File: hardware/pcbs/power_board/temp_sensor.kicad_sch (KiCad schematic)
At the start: 2 parts, among them U14 TMP1075D

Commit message: power_board: final version
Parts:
- C39: LCSC (none) -> C49678
- U14: LCSC (none) -> C2878381
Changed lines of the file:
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@@
+			)
+		)
+		(property "LCSC" "C49678"
+			(at 116.84 96.52 0)
+			(effects
+				(font
+					(size 1.27 1.27)
+				)
+				(hide yes)
 			)
 		)
@@
 			(at 149.86 96.52 0)
 			(effects
+				(font
+					(size 1.27 1.27)
+				)
+				(hide yes)
+			)
+		)
+		(property "LCSC" "C2878381"
+			(at 149.86 96.52 0)
+			(effects

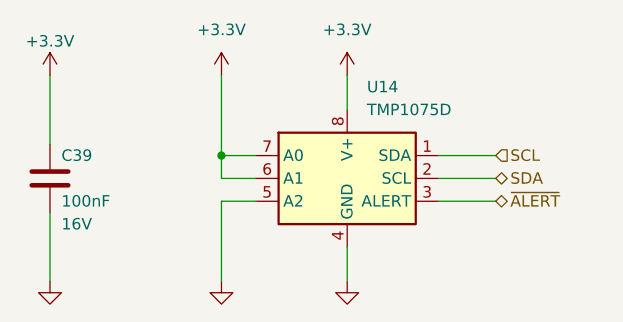
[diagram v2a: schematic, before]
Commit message: power_board: update components to new versions and annotate
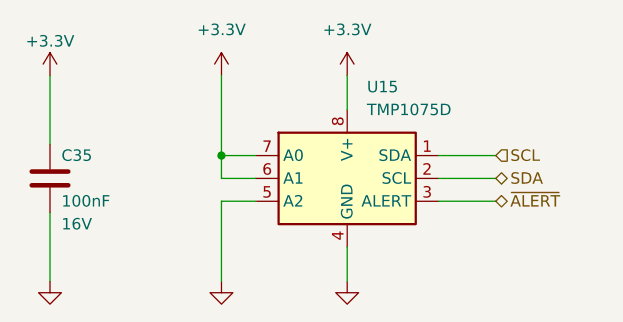
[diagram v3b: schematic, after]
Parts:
- U15: renamed from U14; Part (none) -> TMP1075DR
- renumbered C39 to C35
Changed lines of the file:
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@@
 		(dnp no)
 		(fields_autoplaced yes)
-		(property "Reference" "#PWR0102"
+		(property "Reference" "#PWR093"
 			(at 149.86 88.9 0)
 			(effects
@@
 			(project "power_board"
 				(path "/4b166175-80a4-48c6-994d-6e62a6160b87/cdb98711-4c38-429d-bf0b-859e4979d12f"
-					(reference "#PWR0102")
+					(reference "#PWR093")
 					(unit 1)
 				)
@@
 		(on_board yes)
 		(dnp no)
-		(property "Reference" "C39"
+		(property "Reference" "C35"
 			(at 118.11 93.98 0)
 			(effects
@@
 			(project "power_board"
 				(path "/4b166175-80a4-48c6-994d-6e62a6160b87/cdb98711-4c38-429d-bf0b-859e4979d12f"
-					(reference "C39")
+					(reference "C35")
 					(unit 1)
 				)
@@
 		(dnp no)
 		(fields_autoplaced yes)
-		(property "Reference" "#PWR0103"
+		(property "Reference" "#PWR094"
 			(at 149.86 114.3 0)
 			(effects
@@
 			(project "power_board"
 				(path "/4b166175-80a4-48c6-994d-6e62a6160b87/cdb98711-4c38-429d-bf0b-859e4979d12f"
-					(reference "#PWR0103")
+					(reference "#PWR094")
 					(unit 1)
 				)
@@
 		(dnp no)
 		(fields_autoplaced yes)
-		(property "Reference" "U14"
+		(property "Reference" "U15"
 			(at 152.0541 86.36 0)
 			(effects
@@
 			)
 		)
+		(property "Part" "TMP1075DR "
+			(at 149.86 96.52 0)
+			(effects
+				(font
+					(size 1.27 1.27)
+				)
+				(hide yes)
+			)
+		)
 		(pin "4"
 		)
@@
 			(project "power_board"
 				(path "/4b166175-80a4-48c6-994d-6e62a6160b87/cdb98711-4c38-429d-bf0b-859e4979d12f"
-					(reference "U14")
+					(reference "U15")
 					(unit 1)
 				)
@@
 		(on_board yes)
 		(dnp no)
-		(property "Reference" "#PWR098"
+		(property "Reference" "#PWR089"
 			(at 116.84 88.9 0)
 			(effects
@@
 			(project "power_board"
 				(path "/4b166175-80a4-48c6-994d-6e62a6160b87/cdb98711-4c38-429d-bf0b-859e4979d12f"
-					(reference "#PWR098")
+					(reference "#PWR089")
 					(unit 1)
 				)
@@
 		(dnp no)
 		(fields_autoplaced yes)
-		(property "Reference" "#PWR099"
+		(property "Reference" "#PWR090"
 			(at 116.84 114.3 0)
 			(effects
@@
 			(project "power_board"
 				(path "/4b166175-80a4-48c6-994d-6e62a6160b87/cdb98711-4c38-429d-bf0b-859e4979d12f"
-					(reference "#PWR099")
+					(reference "#PWR090")
 					(unit 1)
 				)
@@
 		(dnp no)
 		(fields_autoplaced yes)
-		(property "Reference" "#PWR0100"
+		(property "Reference" "#PWR091"
 			(at 135.89 88.9 0)
 			(effects
@@
 			(project "power_board"
 				(path "/4b166175-80a4-48c6-994d-6e62a6160b87/cdb98711-4c38-429d-bf0b-859e4979d12f"
-					(reference "#PWR0100")
+					(reference "#PWR091")
 					(unit 1)
 				)
@@
 		(dnp no)
 		(fields_autoplaced yes)
-		(property "Reference" "#PWR0101"
+		(property "Reference" "#PWR092"
 			(at 135.89 114.3 0)
 			(effects
@@
 			(project "power_board"
 				(path "/4b166175-80a4-48c6-994d-6e62a6160b87/cdb98711-4c38-429d-bf0b-859e4979d12f"
-					(reference "#PWR0101")
-					(unit 1)
-				)
+					(reference "#PWR092")
+					(unit 1)
+				)

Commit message: audio_board, power_board: update shop and part links
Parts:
- C35: Part (none) -> C 100nF 16V 0805
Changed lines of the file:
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@@
+			)
+		)
+		(property "Part" "C 100nF 16V 0805"
+			(at 116.84 96.52 0)
+			(effects
+				(font
+					(size 1.27 1.27)
+				)
+				(hide yes)
 			)
 		)

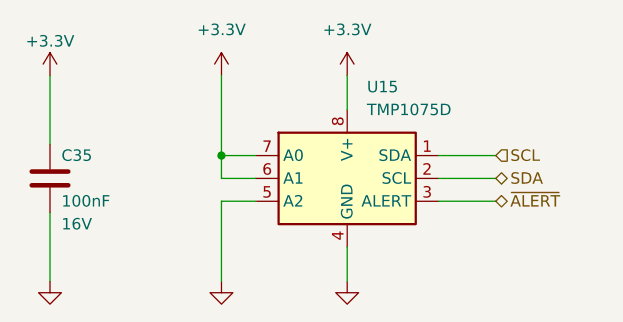
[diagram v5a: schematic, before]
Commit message: boards: fix many silly bugs discovered during testing
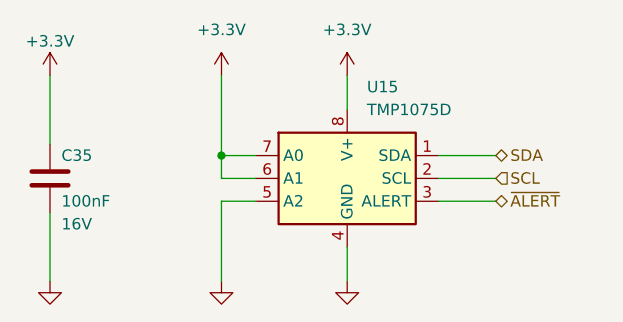
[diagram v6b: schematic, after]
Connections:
- net SCL: now also U15.2 (SCL); no longer U15.1 (SDA)
- net SDA: now also U15.1 (SDA); no longer U15.2 (SCL)
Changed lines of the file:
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@@
 	(hierarchical_label "SCL"
 		(shape input)
-		(at 166.37 93.98 0)
+		(at 166.37 96.52 0)
 		(fields_autoplaced yes)
 		(effects
@@
 	(hierarchical_label "SDA"
 		(shape bidirectional)
-		(at 166.37 96.52 0)
+		(at 166.37 93.98 0)
 		(fields_autoplaced yes)
 		(effects

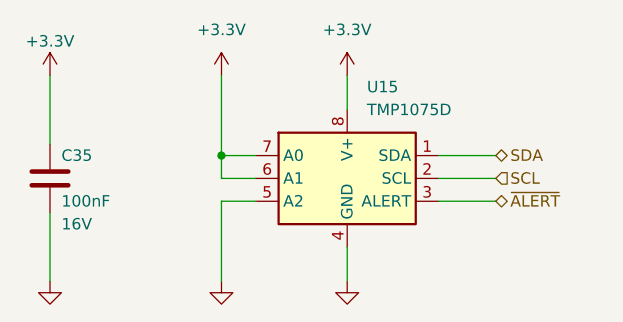
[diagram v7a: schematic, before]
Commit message: power_board: axe one fan output to make space for caps
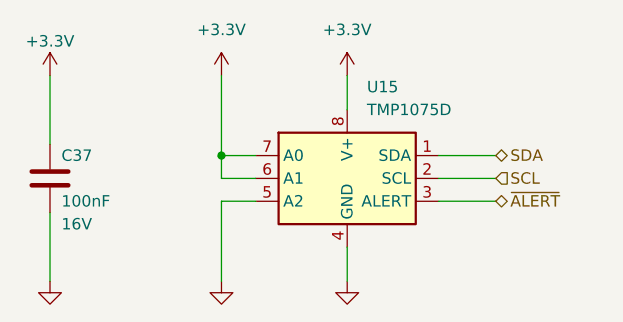
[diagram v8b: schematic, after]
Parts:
- renumbered C35 to C37
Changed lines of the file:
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@@
 		(dnp no)
 		(fields_autoplaced yes)
-		(property "Reference" "#PWR091"
+		(property "Reference" "#PWR092"
 			(at 149.86 88.9 0)
 			(effects
@@
 			(project "power_board"
 				(path "/4b166175-80a4-48c6-994d-6e62a6160b87/cdb98711-4c38-429d-bf0b-859e4979d12f"
-					(reference "#PWR091")
+					(reference "#PWR092")
 					(unit 1)
 				)
@@
 		(on_board yes)
 		(dnp no)
-		(property "Reference" "C35"
+		(property "Reference" "C37"
 			(at 118.11 93.98 0)
 			(effects
@@
 			(project "power_board"
 				(path "/4b166175-80a4-48c6-994d-6e62a6160b87/cdb98711-4c38-429d-bf0b-859e4979d12f"
-					(reference "C35")
+					(reference "C37")
 					(unit 1)
 				)
@@
 		(dnp no)
 		(fields_autoplaced yes)
-		(property "Reference" "#PWR092"
+		(property "Reference" "#PWR093"
 			(at 149.86 114.3 0)
 			(effects
@@
 			(project "power_board"
 				(path "/4b166175-80a4-48c6-994d-6e62a6160b87/cdb98711-4c38-429d-bf0b-859e4979d12f"
-					(reference "#PWR092")
+					(reference "#PWR093")
 					(unit 1)
 				)
@@
 		(on_board yes)
 		(dnp no)
-		(property "Reference" "#PWR087"
+		(property "Reference" "#PWR088"
 			(at 116.84 88.9 0)
 			(effects
@@
 			(project "power_board"
 				(path "/4b166175-80a4-48c6-994d-6e62a6160b87/cdb98711-4c38-429d-bf0b-859e4979d12f"
-					(reference "#PWR087")
+					(reference "#PWR088")
 					(unit 1)
 				)
@@
 		(dnp no)
 		(fields_autoplaced yes)
-		(property "Reference" "#PWR088"
+		(property "Reference" "#PWR089"
 			(at 116.84 114.3 0)
 			(effects
@@
 			(project "power_board"
 				(path "/4b166175-80a4-48c6-994d-6e62a6160b87/cdb98711-4c38-429d-bf0b-859e4979d12f"
-					(reference "#PWR088")
+					(reference "#PWR089")
 					(unit 1)
 				)
@@
 		(dnp no)
 		(fields_autoplaced yes)
-		(property "Reference" "#PWR089"
+		(property "Reference" "#PWR090"
 			(at 135.89 88.9 0)
 			(effects
@@
 			(project "power_board"
 				(path "/4b166175-80a4-48c6-994d-6e62a6160b87/cdb98711-4c38-429d-bf0b-859e4979d12f"
-					(reference "#PWR089")
+					(reference "#PWR090")
 					(unit 1)
 				)
@@
 		(dnp no)
 		(fields_autoplaced yes)
-		(property "Reference" "#PWR090"
+		(property "Reference" "#PWR091"
 			(at 135.89 114.3 0)
 			(effects
@@
 			(project "power_board"
 				(path "/4b166175-80a4-48c6-994d-6e62a6160b87/cdb98711-4c38-429d-bf0b-859e4979d12f"
-					(reference "#PWR090")
-					(unit 1)
-				)
+					(reference "#PWR091")
+					(unit 1)
+				)
